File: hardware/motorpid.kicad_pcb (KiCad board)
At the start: 2 copper layers, 170 x 120 mm, 108 parts, among them J1 BNC, J2 BNC, J3 BNC, J4 MOTOR + - shield, J5 POT 1 (+) 2 (wiper) 3 (-), J6 +15 / GND / -15, Q1 MJB44H11, Q2 MJB45H11, SW1 TARGET SOURCE, SW2 LOOP, SW3 D IN / OFF, SW4 I IN / OFF, SW5 D CAPACITOR, U1 LM321, U2 LM321, U3 LM321, U4 LM321, U5 LM321, U6 LM321, U7 LM321

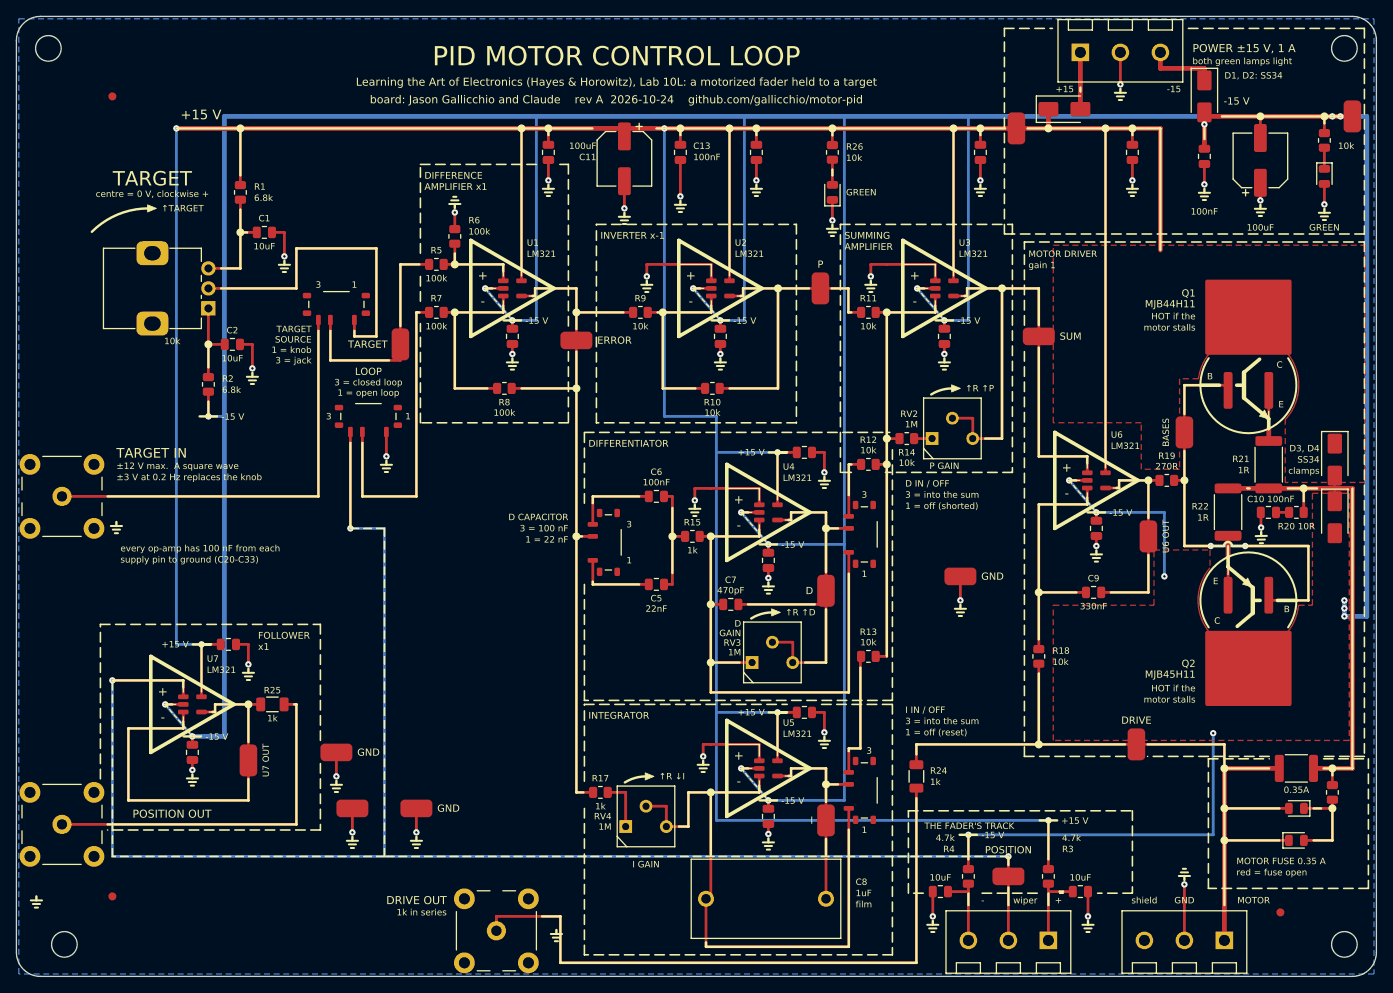
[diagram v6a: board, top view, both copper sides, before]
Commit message: Review round 1 closed: Gemini-4-Argon's and KimiK3's findings applied (RV1's JLCPCB rotation, the fuse's stall story and its 60 V grade, rail clamps D5/D6, the LM321's real swing, step metrics that name the dead band, silk dots and boxes, kienv and the sim's netlist, a deterministic sheet)
- RV1 (C351173): +270 and (3.5, -2.5); JLCPCB's drawing overlaid by the new CPL lands on our pins
- F1: LUTE 1812L035/60GR (C18198330), same hold/trip/R; every document now says a short opens it
  in about a second and a full-drive stall (0.61 A, between hold and trip) may take minutes or never
- D5, D6 (SS34) clamp each rail to ground: one rail left open cannot reverse-bias its electrolytic
- sim: LM321 output 2 V from each rail (D rule 239k, stall 0.61 A, step drive 11.7 V); step metrics
  report peak, swing back and rest separately; the sim stage exports its own netlist
- silk: dot where the dashed POSITION branches and at the track's end capacitors; C3/C4 inside
  their box; the -15 V flag clear of the title; D2PAK emitter copper at full width
- docs: the book's real "not 411", knob direction settled, scope grounds on GND loops only,
  x10 probes, the gains recipe's switches and signs, the rail-sag rest offset with the jack
- build: KiCad 9 on PATH no longer wins; rectangles' UUIDs hashed (byte-identical sheet);
  check messages from the sim; stock from the BOM; dead limiter parts removed
- the two reviews committed (the Fable-labelled one renamed KimiK3, Jason to confirm the
  model; datasheet excerpts kept out of git); the reviews README and the brief updated
- ERC 0, 258 checks, DRC 0, thermal 120/122 C, fab checks, 31/31 claims

Co-Authored-By: Claude Opus 5.5 <noreply@anthropic.com>
Claude-Session: https://claude.ai/code/session_017Q2PYKR2UewvTfQgKmRJsG
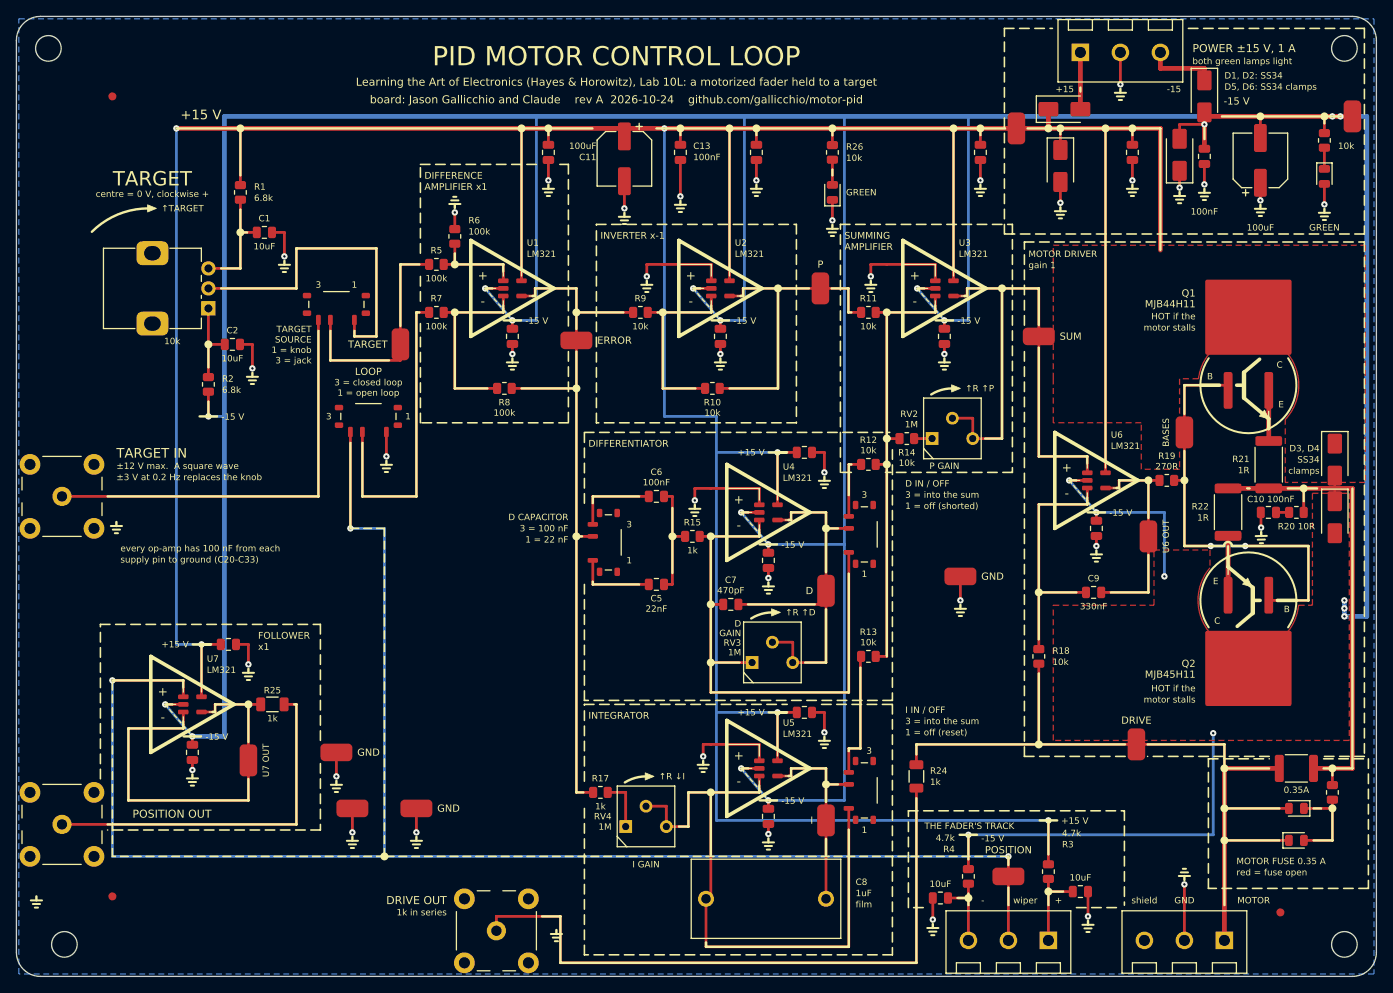
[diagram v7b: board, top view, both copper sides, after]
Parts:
- added D5: SS34, Diode_SMD:D_SMA, F.Cu at (130.5, 18.7)
- added D6: SS34, Diode_SMD:D_SMA, F.Cu at (145.4, 17.3)
- moved C4 0.80 mm to (115.5, 110.2)
- moved R3 0.60 mm to (129.0, 106.9)
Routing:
- net -15V: track 624.5 -> 629.4 mm
- net GND: track 139.7 -> 144.0 mm, vias 37 -> 39
- net +15V: track 511.1 -> 513.2 mm
- net /POT+: track 10.1 -> 10.7 mm
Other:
- board text added: "A short to GND opens the fuse in about a second (red lamps); it resets."
- board text added: "A stall may never open it: HOT copper reaches 90 C, so use the standoffs."
- board text added: "D5, D6: SS34 clamps"
- board text added: "Scope ground clips go on the GND loops only, never on a signal or a rail."
- board text removed: "A stall at a few volts does not: HOT copper reaches 90 C, so use the standoffs."
- board text removed: "A stall at full drive or a short to GND opens the fuse (red lamps); it resets."

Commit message: Rev A pre-order checks from the newer lessons; BOARD_DATE 2026-10-29: the screw terminals turned (KF301 wire face 3.6 mm from the pins, JLCPCB's drawing +180), PLACEMENT_CHECKS prints every row (J3, J6, D3-D6), assembly drawings fitted to Letter, check_rotations.py (fit and the upload laid on our pads) and check_pinouts.py, the switches' datum 0.25 mm; chat log Response 14
Co-Authored-By: Claude Opus 5.5 <noreply@anthropic.com>
Claude-Session: https://claude.ai/code/session_017Q2PYKR2UewvTfQgKmRJsG
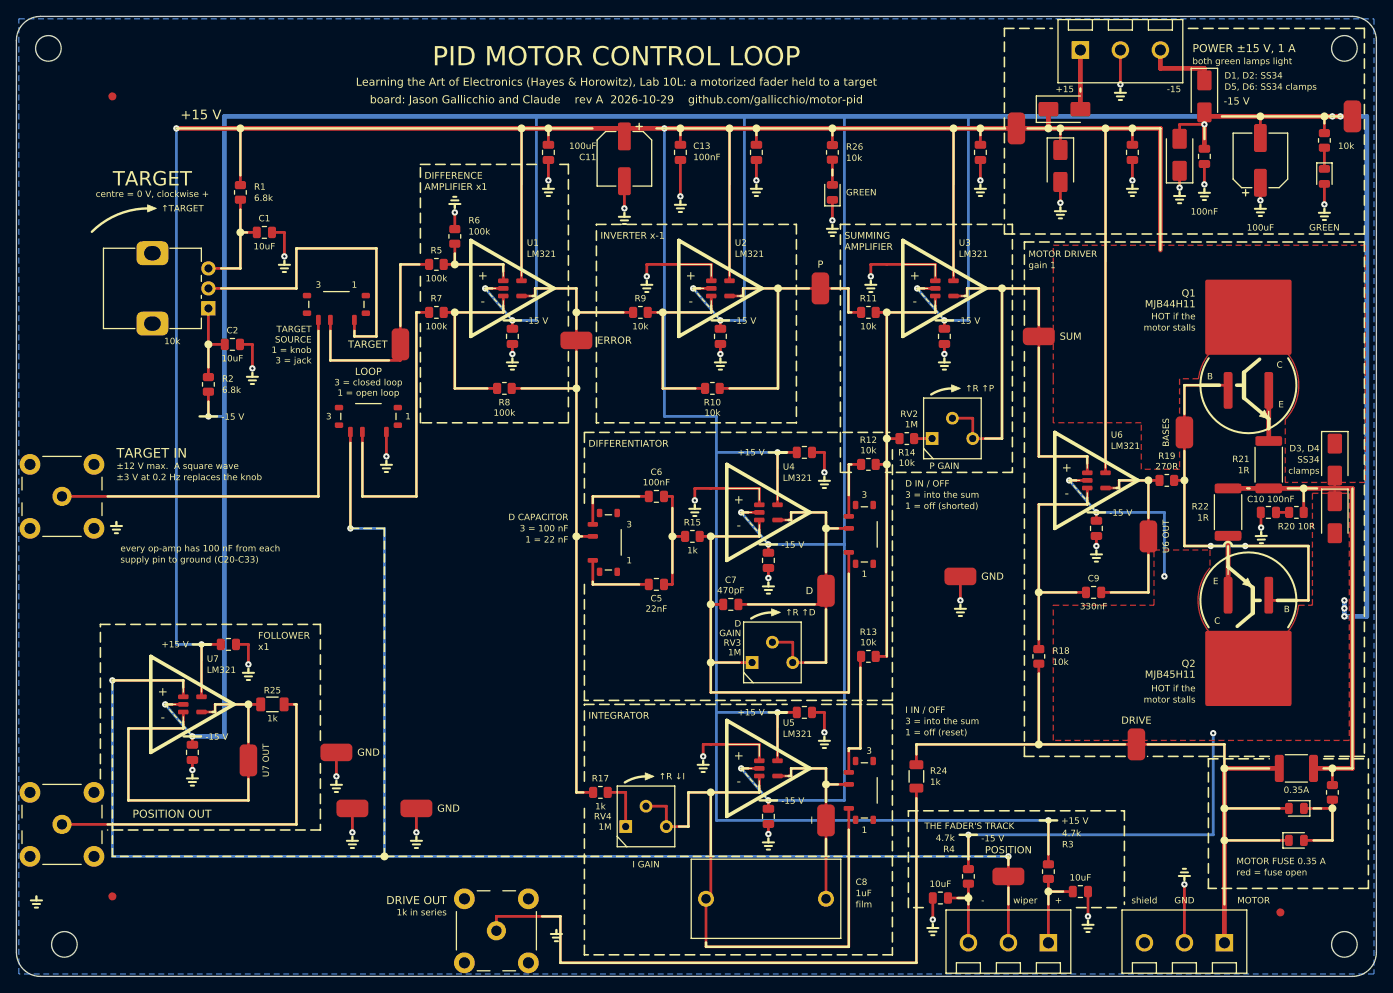
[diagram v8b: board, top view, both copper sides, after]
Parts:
- moved J6 0.30 mm to (138.0, 4.20)
- moved J4 0.30 mm to (146.0, 115.8)
- moved J5 0.30 mm to (124.0, 115.8)
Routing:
- net GND: track 144.0 -> 144.6 mm
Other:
- board text added: "Jason Gallicchio and Claude, rev A, 2026-10-29"
- board text added: "board: Jason Gallicchio and Claude rev A 2026-10-29 github.com/gallicchio/motor-pid"
- board text removed: "Jason Gallicchio and Claude, rev A, 2026-10-24"
- board text removed: "board: Jason Gallicchio and Claude rev A 2026-10-24 github.com/gallicchio/motor-pid"
